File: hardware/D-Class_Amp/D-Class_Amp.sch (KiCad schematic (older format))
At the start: 3 parts, among them J101 AudioJack2

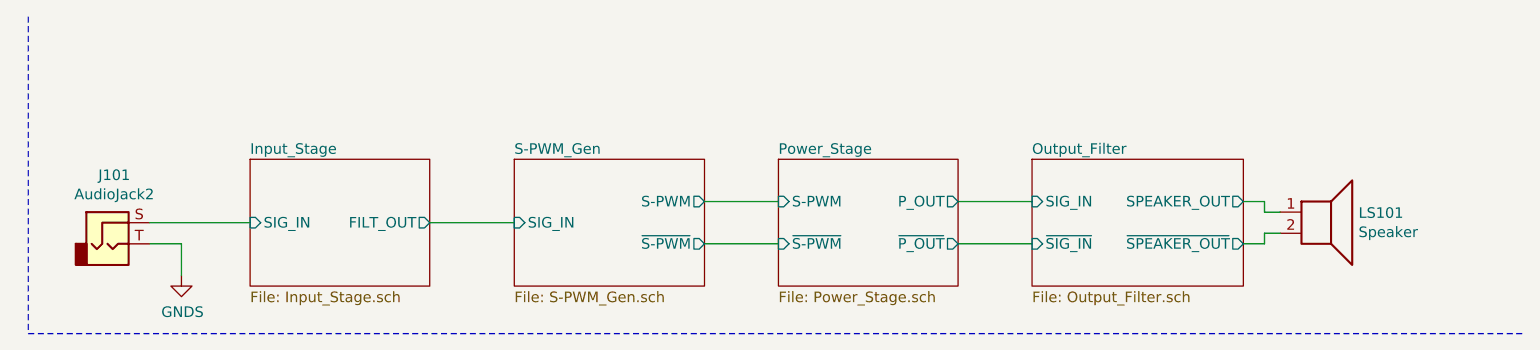
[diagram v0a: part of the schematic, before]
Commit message: updated SPWM model with new comparators, also added test points to schematic and fixed MOSFET footprints
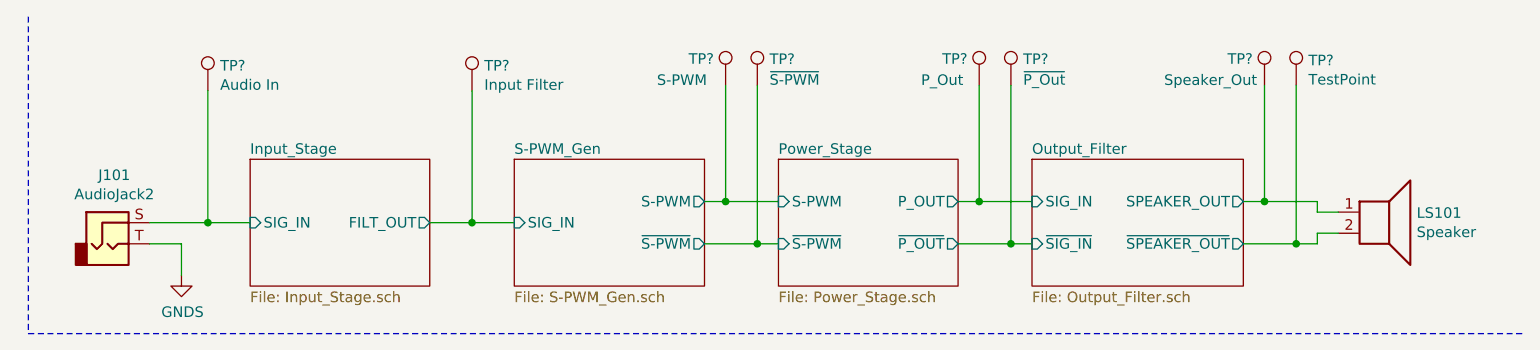
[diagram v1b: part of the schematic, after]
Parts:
- added TP?: Audio In, TestPoint:TestPoint_THTPad_D2.0mm_Drill1.0mm, symbol Connector:TestPoint
- added TP?: Input Filter, TestPoint:TestPoint_THTPad_D2.0mm_Drill1.0mm, symbol Connector:TestPoint
- added TP?: ~S-PWM, TestPoint:TestPoint_THTPad_D2.0mm_Drill1.0mm, symbol Connector:TestPoint
- added TP?: S-PWM, TestPoint:TestPoint_THTPad_D2.0mm_Drill1.0mm, symbol Connector:TestPoint
- added TP?: P_Out, TestPoint:TestPoint_THTPad_D2.0mm_Drill1.0mm, symbol Connector:TestPoint
- added TP?: ~P_Out, TestPoint:TestPoint_THTPad_D2.0mm_Drill1.0mm, symbol Connector:TestPoint
- added TP?: Speaker_Out, TestPoint:TestPoint_THTPad_D2.0mm_Drill1.0mm, symbol Connector:TestPoint
- added TP?: TestPoint, TestPoint:TestPoint_THTPad_D2.0mm_Drill1.0mm, symbol Connector:TestPoint
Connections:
- net Input_Stage/FILT_OUT: now also TP?.1
- net Input_Stage/SIG_IN: now also TP?.1
- net Output_Filter/SIG_IN: now also TP?.1
- net Output_Filter/SPEAKER_OUT: now also TP?.1
- net Output_Filter/~SIG_IN: now also TP?.1
- net Output_Filter/~SPEAKER_OUT: now also TP?.1
- net Power_Stage/S-PWM: now also TP?.1
- net Power_Stage/~S-PWM: now also TP?.1
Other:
- moved on the sheet: LS101
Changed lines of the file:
@@
 $EndSheet
+$Sheet
+S 6475 1150 900  600
+U 61049843
+F0 "S-PWM_Gen" 50
+F1 "S-PWM_Gen.sch" 50
+F2 "S-PWM" O R 7375 1350 50
+F3 "~S-PWM" O R 7375 1550 50
+F4 "SIG_IN" I L 6475 1450 50
+$EndSheet
+Wire Wire Line
+	6075 1450 6275 1450
+Wire Wire Line
+	10275 1350 10275 1400
+Wire Wire Line
+	10275 1550 10275 1500
+$Comp
+L Connector:AudioJack2 J101
+U 1 1 611DD9A4
+P 4550 1550
+F 0 "J101" H 4582 1875 50  0000 C CNN
+F 1 "AudioJack2" H 4582 1784 50  0000 C CNN
+F 2 "" H 4550 1550 50  0001 C CNN
+F 3 "~" H 4550 1550 50  0001 C CNN
+	1    4550 1550
+	1    0    0    -1
+$EndComp
+Wire Wire Line
+	4750 1450 5025 1450
+$Comp
+L power:GNDS #PWR0103
+U 1 1 611DE882
+P 4900 1700
+F 0 "#PWR0103" H 4900 1450 50  0001 C CNN
+F 1 "GNDS" H 4905 1527 50  0000 C CNN
+F 2 "" H 4900 1700 50  0001 C CNN
+F 3 "" H 4900 1700 50  0001 C CNN
+	1    4900 1700
+	1    0    0    -1
+$EndComp
+Wire Wire Line
+	4750 1550 4900 1550
+Wire Wire Line
+	4900 1550 4900 1700
+Wire Notes Line
+	4175 475  4175 1975
+Wire Notes Line
+	4175 1975 11250 1975
+$Comp
+L power:GNDS #PWR0102
+U 1 1 612A4FBB
+P 1575 1400
+F 0 "#PWR0102" H 1575 1150 50  0001 C CNN
+F 1 "GNDS" H 1580 1227 50  0000 C CNN
+F 2 "" H 1575 1400 50  0001 C CNN
+F 3 "" H 1575 1400 50  0001 C CNN
+	1    1575 1400
+	1    0    0    -1
+$EndComp
+$Comp
+L power:GND #PWR0101
+U 1 1 612A56C1
+P 1225 1400
+F 0 "#PWR0101" H 1225 1150 50  0001 C CNN
+F 1 "GND" H 1230 1227 50  0000 C CNN
+F 2 "" H 1225 1400 50  0001 C CNN
+F 3 "" H 1225 1400 50  0001 C CNN
+	1    1225 1400
+	1    0    0    -1
+$EndComp
+$Comp
+L Device:Net-Tie_2 NT101
+U 1 1 612A676E
+P 1400 1325
+F 0 "NT101" H 1400 1506 50  0000 C CNN
+F 1 "Net-Tie_2" H 1400 1415 50  0000 C CNN
+F 2 "" H 1400 1325 50  0001 C CNN
+F 3 "~" H 1400 1325 50  0001 C CNN
+	1    1400 1325
+	1    0    0    -1
+$EndComp
+Wire Wire Line
+	1225 1400 1225 1325
+Wire Wire Line
+	1225 1325 1300 1325
+Wire Wire Line
+	1500 1325 1575 1325
+Wire Wire Line
+	1575 1325 1575 1400
+$Comp
+L Connector:TestPoint TP?
+U 1 1 61126C37
+P 5025 825
+F 0 "TP?" H 5083 943 50  0000 L CNN
+F 1 "Audio In" H 5083 852 50  0000 L CNN
+F 2 "TestPoint:TestPoint_THTPad_D2.0mm_Drill1.0mm" H 5225 825 50  0001 C CNN
+F 3 "~" H 5225 825 50  0001 C CNN
+	1    5025 825
+	1    0    0    -1
+$EndComp
+$Comp
+L Connector:TestPoint TP?
+U 1 1 6112780B
+P 6275 825
+F 0 "TP?" H 6333 943 50  0000 L CNN
+F 1 "Input Filter" H 6333 852 50  0000 L CNN
+F 2 "TestPoint:TestPoint_THTPad_D2.0mm_Drill1.0mm" H 6475 825 50  0001 C CNN
+F 3 "~" H 6475 825 50  0001 C CNN
+	1    6275 825
+	1    0    0    -1
+$EndComp
+Wire Wire Line
+	9925 1550 10175 1550
+Wire Wire Line
+	9925 1350 10025 1350
+Wire Wire Line
+	8575 1550 8825 1550
+Wire Wire Line
+	8575 1350 8675 1350
+$Sheet
+S 8925 1150 1000 600
+U 610497C9
+F0 "Output_Filter" 50
+F1 "Output_Filter.sch" 50
+F2 "SIG_IN" I L 8925 1350 50
+F3 "~SIG_IN" I L 8925 1550 50
+F4 "SPEAKER_OUT" O R 9925 1350 50
+F5 "~SPEAKER_OUT" O R 9925 1550 50
+$EndSheet
+Wire Wire Line
+	10275 1500 10375 1500
+Wire Wire Line
+	10275 1400 10375 1400
+$Comp
+L Device:Speaker LS101
+U 1 1 61193870
+P 10575 1400
+F 0 "LS101" H 10745 1396 50  0000 L CNN
+F 1 "Speaker" H 10745 1305 50  0000 L CNN
+F 2 "" H 10575 1200 50  0001 C CNN
+F 3 "~" H 10565 1350 50  0001 C CNN
+	1    10575 1400
+	1    0    0    -1
+$EndComp
+$Comp
+L Connector:TestPoint TP?
+U 1 1 6112B1A8
+P 7475 800
+F 0 "TP?" H 7300 925 50  0000 L CNN
+F 1 "S-PWM" H 7150 825 50  0000 L CNN
+F 2 "TestPoint:TestPoint_THTPad_D2.0mm_Drill1.0mm" H 7675 800 50  0001 C CNN
+F 3 "~" H 7675 800 50  0001 C CNN
+	1    7475 800
+	1    0    0    -1
+$EndComp
+$Comp
+L Connector:TestPoint TP?
+U 1 1 61129DBB
+P 7625 800
+F 0 "TP?" H 7683 924 50  0000 L CNN
+F 1 "~S-PWM" H 7683 826 50  0000 L CNN
+F 2 "TestPoint:TestPoint_THTPad_D2.0mm_Drill1.0mm" H 7825 800 50  0001 C CNN
+F 3 "~" H 7825 800 50  0001 C CNN
+	1    7625 800
+	1    0    0    -1
+$EndComp
+$Comp
+L Connector:TestPoint TP?
+U 1 1 6112D71A
+P 8675 800
+F 0 "TP?" H 8500 925 50  0000 L CNN
+F 1 "P_Out" H 8400 825 50  0000 L CNN
+F 2 "TestPoint:TestPoint_THTPad_D2.0mm_Drill1.0mm" H 8875 800 50  0001 C CNN
+F 3 "~" H 8875 800 50  0001 C CNN
+	1    8675 800
+	1    0    0    -1
+$EndComp
+$Comp
+L Connector:TestPoint TP?
+U 1 1 6112D764
+P 8825 800
+F 0 "TP?" H 8883 924 50  0000 L CNN
+F 1 "~P_Out" H 8883 826 50  0000 L CNN
+F 2 "TestPoint:TestPoint_THTPad_D2.0mm_Drill1.0mm" H 9025 800 50  0001 C CNN
+F 3 "~" H 9025 800 50  0001 C CNN
+	1    8825 800
+	1    0    0    -1
+$EndComp
+Wire Wire Line
+	8675 800  8675 1350
+Connection ~ 8675 1350
+Wire Wire Line
+	8675 1350 8925 1350
+Wire Wire Line
+	8825 800  8825 1550
+Connection ~ 8825 1550
+Wire Wire Line
+	8825 1550 8925 1550
+Wire Wire Line
+	7375 1350 7475 1350
 $Sheet
 S 7725 1150 850  600
@@
 F5 "~P_OUT" O R 8575 1550 50
 $EndSheet
-$Sheet
-S 8925 1150 1000 600
-U 610497C9
-F0 "Output_Filter" 50
-F1 "Output_Filter.sch" 50
-F2 "SIG_IN" I L 8925 1350 50
-F3 "~SIG_IN" I L 8925 1550 50
-F4 "SPEAKER_OUT" O R 9925 1350 50
-F5 "~SPEAKER_OUT" O R 9925 1550 50
-$EndSheet
-$Sheet
-S 6475 1150 900  600
-U 61049843
-F0 "S-PWM_Gen" 50
-F1 "S-PWM_Gen.sch" 50
-F2 "S-PWM" O R 7375 1350 50
-F3 "~S-PWM" O R 7375 1550 50
-F4 "SIG_IN" I L 6475 1450 50
-$EndSheet
-Wire Wire Line
-	6075 1450 6475 1450
-Wire Wire Line
-	7375 1350 7725 1350
-Wire Wire Line
-	7375 1550 7725 1550
-$Comp
-L Device:Speaker LS101
-U 1 1 61193870
-P 10300 1400
-F 0 "LS101" H 10470 1396 50  0000 L CNN
-F 1 "Speaker" H 10470 1305 50  0000 L CNN
-F 2 "" H 10300 1200 50  0001 C CNN
-F 3 "~" H 10290 1350 50  0001 C CNN
-	1    10300 1400
-	1    0    0    -1
-$EndComp
-Wire Wire Line
-	8575 1350 8925 1350
-Wire Wire Line
-	9925 1350 10025 1350
-Wire Wire Line
-	10025 1350 10025 1400
-Wire Wire Line
-	10025 1400 10100 1400
-Wire Wire Line
-	9925 1550 10025 1550
-Wire Wire Line
-	10025 1550 10025 1500
-Wire Wire Line
-	10025 1500 10100 1500
-$Comp
-L Connector:AudioJack2 J101
-U 1 1 611DD9A4
-P 4550 1550
-F 0 "J101" H 4582 1875 50  0000 C CNN
-F 1 "AudioJack2" H 4582 1784 50  0000 C CNN
-F 2 "" H 4550 1550 50  0001 C CNN
-F 3 "~" H 4550 1550 50  0001 C CNN
-	1    4550 1550
-	1    0    0    -1
-$EndComp
-Wire Wire Line
-	4750 1450 5225 1450
-$Comp
-L power:GNDS #PWR0103
-U 1 1 611DE882
-P 4900 1700
-F 0 "#PWR0103" H 4900 1450 50  0001 C CNN
-F 1 "GNDS" H 4905 1527 50  0000 C CNN
-F 2 "" H 4900 1700 50  0001 C CNN
-F 3 "" H 4900 1700 50  0001 C CNN
-	1    4900 1700
-	1    0    0    -1
-$EndComp
-Wire Wire Line
-	4750 1550 4900 1550
-Wire Wire Line
-	4900 1550 4900 1700
-Wire Wire Line
-	8575 1550 8925 1550
-Wire Notes Line
-	4175 475  4175 1975
-Wire Notes Line
-	4175 1975 11250 1975
-$Comp
-L power:GNDS #PWR0102
-U 1 1 612A4FBB
-P 1575 1400
-F 0 "#PWR0102" H 1575 1150 50  0001 C CNN
-F 1 "GNDS" H 1580 1227 50  0000 C CNN
-F 2 "" H 1575 1400 50  0001 C CNN
-F 3 "" H 1575 1400 50  0001 C CNN
-	1    1575 1400
-	1    0    0    -1
-$EndComp
-$Comp
-L power:GND #PWR0101
-U 1 1 612A56C1
-P 1225 1400
-F 0 "#PWR0101" H 1225 1150 50  0001 C CNN
-F 1 "GND" H 1230 1227 50  0000 C CNN
-F 2 "" H 1225 1400 50  0001 C CNN
-F 3 "" H 1225 1400 50  0001 C CNN
-	1    1225 1400
-	1    0    0    -1
-$EndComp
-$Comp
-L Device:Net-Tie_2 NT101
-U 1 1 612A676E
-P 1400 1325
-F 0 "NT101" H 1400 1506 50  0000 C CNN
-F 1 "Net-Tie_2" H 1400 1415 50  0000 C CNN
-F 2 "" H 1400 1325 50  0001 C CNN
-F 3 "~" H 1400 1325 50  0001 C CNN
-	1    1400 1325
-	1    0    0    -1
-$EndComp
-Wire Wire Line
-	1225 1400 1225 1325
-Wire Wire Line
-	1225 1325 1300 1325
-Wire Wire Line
-	1500 1325 1575 1325
-Wire Wire Line
-	1575 1325 1575 1400
+Wire Wire Line
+	7475 800  7475 1350
+Connection ~ 7475 1350
+Wire Wire Line
+	7475 1350 7725 1350
+Wire Wire Line
+	7625 800  7625 1550
+Wire Wire Line
+	7375 1550 7625 1550
+Connection ~ 7625 1550
+Wire Wire Line
+	7625 1550 7725 1550
+Wire Wire Line
+	6275 825  6275 1450
+Connection ~ 6275 1450
+Wire Wire Line
+	6275 1450 6475 1450
+Wire Wire Line
+	5025 825  5025 1450
+Connection ~ 5025 1450
+Wire Wire Line
+	5025 1450 5225 1450
+$Comp
+L Connector:TestPoint TP?
+U 1 1 611372D5
+P 10025 800
+F 0 "TP?" H 9850 925 50  0000 L CNN
+F 1 "Speaker_Out" H 9550 825 50  0000 L CNN
+F 2 "TestPoint:TestPoint_THTPad_D2.0mm_Drill1.0mm" H 10225 800 50  0001 C CNN
+F 3 "~" H 10225 800 50  0001 C CNN
+	1    10025 800
+	1    0    0    -1
+$EndComp
+$Comp
+L Connector:TestPoint TP?
+U 1 1 6113731F
+P 10175 800
+F 0 "TP?" H 10233 918 50  0000 L CNN
+F 1 "TestPoint" H 10233 827 50  0000 L CNN
+F 2 "TestPoint:TestPoint_THTPad_D2.0mm_Drill1.0mm" H 10375 800 50  0001 C CNN
+F 3 "~" H 10375 800 50  0001 C CNN
+	1    10175 800
+	1    0    0    -1
+$EndComp
+Wire Wire Line
+	10025 800  10025 1350
+Wire Wire Line
+	10175 800  10175 1550
+Connection ~ 10025 1350
+Wire Wire Line
+	10025 1350 10275 1350
+Connection ~ 10175 1550
+Wire Wire Line
+	10175 1550 10275 1550
 $EndSCHEMATC

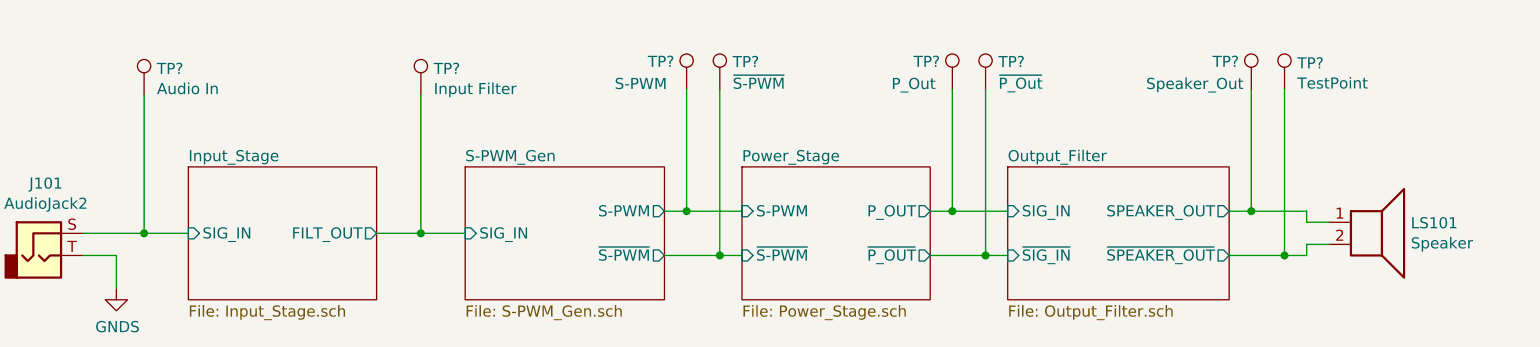
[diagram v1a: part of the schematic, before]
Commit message: Added potentiometer to input gain stage, assigned all input footprints
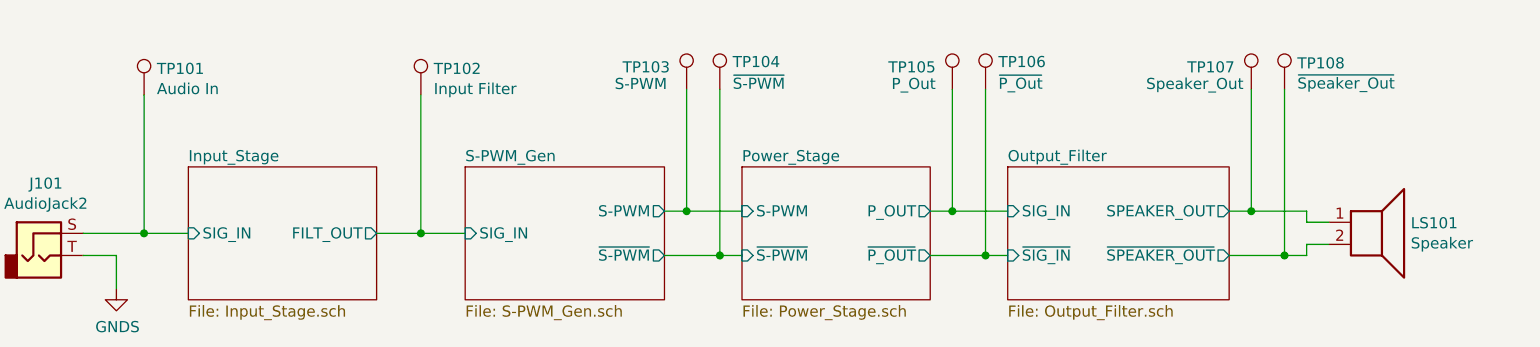
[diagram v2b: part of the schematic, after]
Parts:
- TP108: renamed from TP?; value TestPoint -> ~Speaker_Out
- gave numbers to parts that had none: 7
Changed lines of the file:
@@
 	1575 1325 1575 1400
 $Comp
-L Connector:TestPoint TP?
+L Connector:TestPoint TP101
 U 1 1 61126C37
 P 5025 825
-F 0 "TP?" H 5083 943 50  0000 L CNN
+F 0 "TP101" H 5083 943 50  0000 L CNN
 F 1 "Audio In" H 5083 852 50  0000 L CNN
 F 2 "TestPoint:TestPoint_THTPad_D2.0mm_Drill1.0mm" H 5225 825 50  0001 C CNN
@@
 $EndComp
 $Comp
-L Connector:TestPoint TP?
+L Connector:TestPoint TP102
 U 1 1 6112780B
 P 6275 825
-F 0 "TP?" H 6333 943 50  0000 L CNN
+F 0 "TP102" H 6333 943 50  0000 L CNN
 F 1 "Input Filter" H 6333 852 50  0000 L CNN
 F 2 "TestPoint:TestPoint_THTPad_D2.0mm_Drill1.0mm" H 6475 825 50  0001 C CNN
@@
 $EndComp
 $Comp
-L Connector:TestPoint TP?
-U 1 1 6112B1A8
-P 7475 800
-F 0 "TP?" H 7300 925 50  0000 L CNN
-F 1 "S-PWM" H 7150 825 50  0000 L CNN
-F 2 "TestPoint:TestPoint_THTPad_D2.0mm_Drill1.0mm" H 7675 800 50  0001 C CNN
-F 3 "~" H 7675 800 50  0001 C CNN
-	1    7475 800
-	1    0    0    -1
-$EndComp
-$Comp
-L Connector:TestPoint TP?
+L Connector:TestPoint TP104
 U 1 1 61129DBB
 P 7625 800
-F 0 "TP?" H 7683 924 50  0000 L CNN
+F 0 "TP104" H 7683 924 50  0000 L CNN
 F 1 "~S-PWM" H 7683 826 50  0000 L CNN
 F 2 "TestPoint:TestPoint_THTPad_D2.0mm_Drill1.0mm" H 7825 800 50  0001 C CNN
@@
 $EndComp
 $Comp
-L Connector:TestPoint TP?
+L Connector:TestPoint TP105
 U 1 1 6112D71A
 P 8675 800
-F 0 "TP?" H 8500 925 50  0000 L CNN
+F 0 "TP105" H 8600 900 50  0000 R CNN
 F 1 "P_Out" H 8400 825 50  0000 L CNN
 F 2 "TestPoint:TestPoint_THTPad_D2.0mm_Drill1.0mm" H 8875 800 50  0001 C CNN
@@
 $EndComp
 $Comp
-L Connector:TestPoint TP?
+L Connector:TestPoint TP106
 U 1 1 6112D764
 P 8825 800
-F 0 "TP?" H 8883 924 50  0000 L CNN
+F 0 "TP106" H 8883 924 50  0000 L CNN
 F 1 "~P_Out" H 8883 826 50  0000 L CNN
 F 2 "TestPoint:TestPoint_THTPad_D2.0mm_Drill1.0mm" H 9025 800 50  0001 C CNN
@@
 	5025 1450 5225 1450
 $Comp
-L Connector:TestPoint TP?
-U 1 1 611372D5
-P 10025 800
-F 0 "TP?" H 9850 925 50  0000 L CNN
-F 1 "Speaker_Out" H 9550 825 50  0000 L CNN
-F 2 "TestPoint:TestPoint_THTPad_D2.0mm_Drill1.0mm" H 10225 800 50  0001 C CNN
-F 3 "~" H 10225 800 50  0001 C CNN
-	1    10025 800
-	1    0    0    -1
-$EndComp
-$Comp
-L Connector:TestPoint TP?
+L Connector:TestPoint TP108
 U 1 1 6113731F
 P 10175 800
-F 0 "TP?" H 10233 918 50  0000 L CNN
-F 1 "TestPoint" H 10233 827 50  0000 L CNN
+F 0 "TP108" H 10233 918 50  0000 L CNN
+F 1 "~Speaker_Out" H 10233 827 50  0000 L CNN
 F 2 "TestPoint:TestPoint_THTPad_D2.0mm_Drill1.0mm" H 10375 800 50  0001 C CNN
 F 3 "~" H 10375 800 50  0001 C CNN
@@
 Wire Wire Line
 	10175 1550 10275 1550
+$Comp
+L Connector:TestPoint TP103
+U 1 1 6112B1A8
+P 7475 800
+F 0 "TP103" H 7400 900 50  0000 R CNN
+F 1 "S-PWM" H 7150 825 50  0000 L CNN
+F 2 "TestPoint:TestPoint_THTPad_D2.0mm_Drill1.0mm" H 7675 800 50  0001 C CNN
+F 3 "~" H 7675 800 50  0001 C CNN
+	1    7475 800
+	1    0    0    -1
+$EndComp
+$Comp
+L Connector:TestPoint TP107
+U 1 1 611372D5
+P 10025 800
+F 0 "TP107" H 9950 900 50  0000 R CNN
+F 1 "Speaker_Out" H 9550 825 50  0000 L CNN
+F 2 "TestPoint:TestPoint_THTPad_D2.0mm_Drill1.0mm" H 10225 800 50  0001 C CNN
+F 3 "~" H 10225 800 50  0001 C CNN
+	1    10025 800
+	1    0    0    -1
+$EndComp
 $EndSCHEMATC

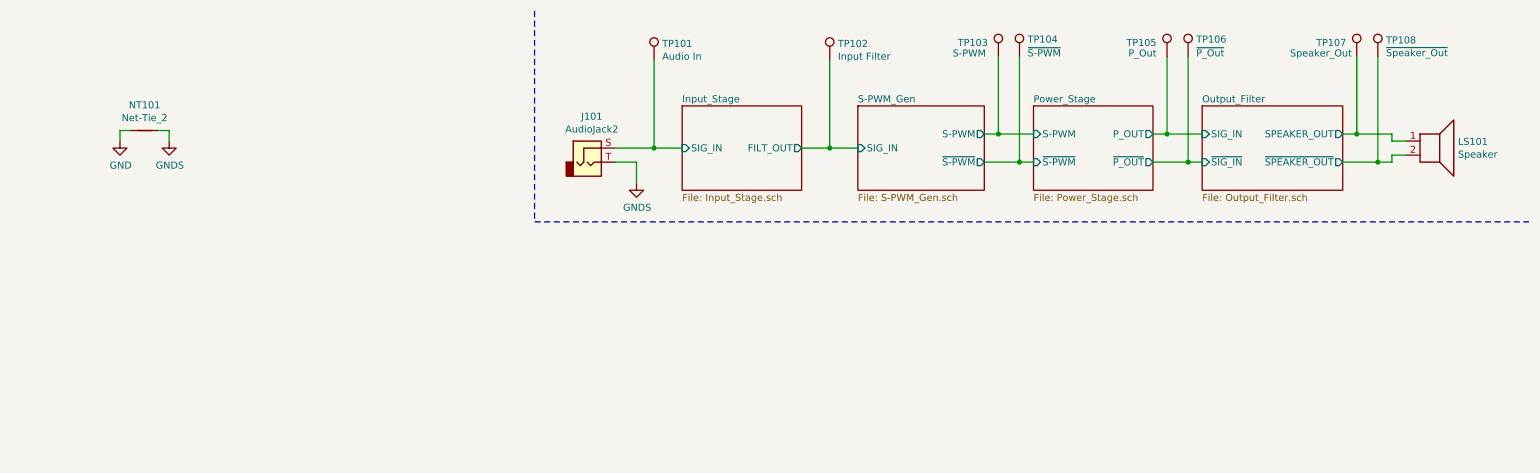
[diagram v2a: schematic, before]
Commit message: added the 5V regulator and updated footprints
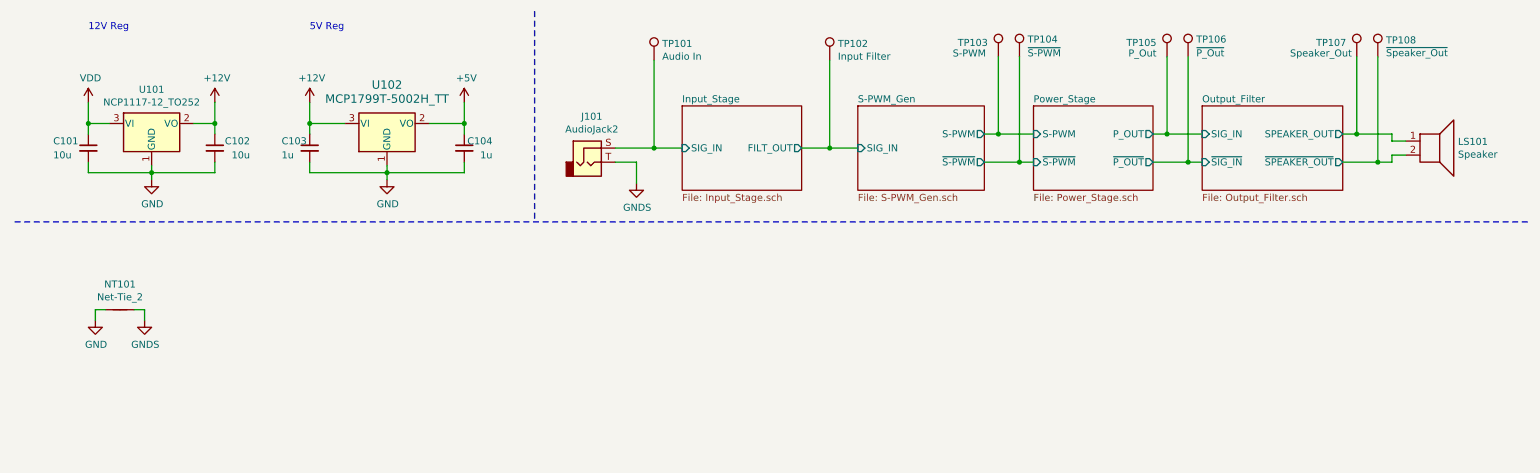
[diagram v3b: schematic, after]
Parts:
- added C101, C102: 10u, Capacitor_SMD:C_0805_2012Metric_Pad1.18x1.45mm_HandSolder, symbol Device:C_Small
- added C103, C104: 1u, Capacitor_SMD:C_0805_2012Metric_Pad1.18x1.45mm_HandSolder, symbol Device:C_Small
- added U101: NCP1117-12_TO252, Package_TO_SOT_SMD:TO-252-2, symbol Regulator_Linear:NCP1117-12_TO252
- added U102: MCP1799T-5002H_TT, SOT-23_TT_MCH, symbol MCP1799T:MCP1799T-5002H_TT
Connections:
- net GND: now also C101.2, C102.2, C103.2, C104.2, U101.1 (GND), U102.1 (GND)
- new net +12V: C102.1, C103.1, U101.2 (VO), U102.3 (VI)
- new net +5V: C104.1, U102.2 (VO)
- new net VDD: C101.1, U101.3 (VI)
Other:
- note added: "12V Reg\n\n"
- note added: "5V Reg\n\n"
- moved on the sheet: NT101

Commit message: added footprint to 5V reg
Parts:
- U102: footprint SOT-23_TT_MCH -> Package_TO_SOT_SMD:SOT-23_Handsoldering
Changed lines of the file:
@@
 F 0 "U102" H 3125 1650 60  0000 C CNN
 F 1 "MCP1799T-5002H_TT" H 3125 1550 60  0000 C CNN
-F 2 "SOT-23_TT_MCH" H 3925 1565 60  0001 C CNN
+F 2 "Package_TO_SOT_SMD:SOT-23_Handsoldering" H 3925 1565 60  0001 C CNN
 F 3 "" H 3125 1325 60  0000 C CNN
 	1    3125 1325
